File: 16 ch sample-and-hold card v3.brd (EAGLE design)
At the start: 77.2 x 24.8 mm, 32 parts, among them IC2 TL074D, IC3 TL074D, IC4 TL074D, IC5 TL074D, IC6 DG408DY, IC7 DG408DY

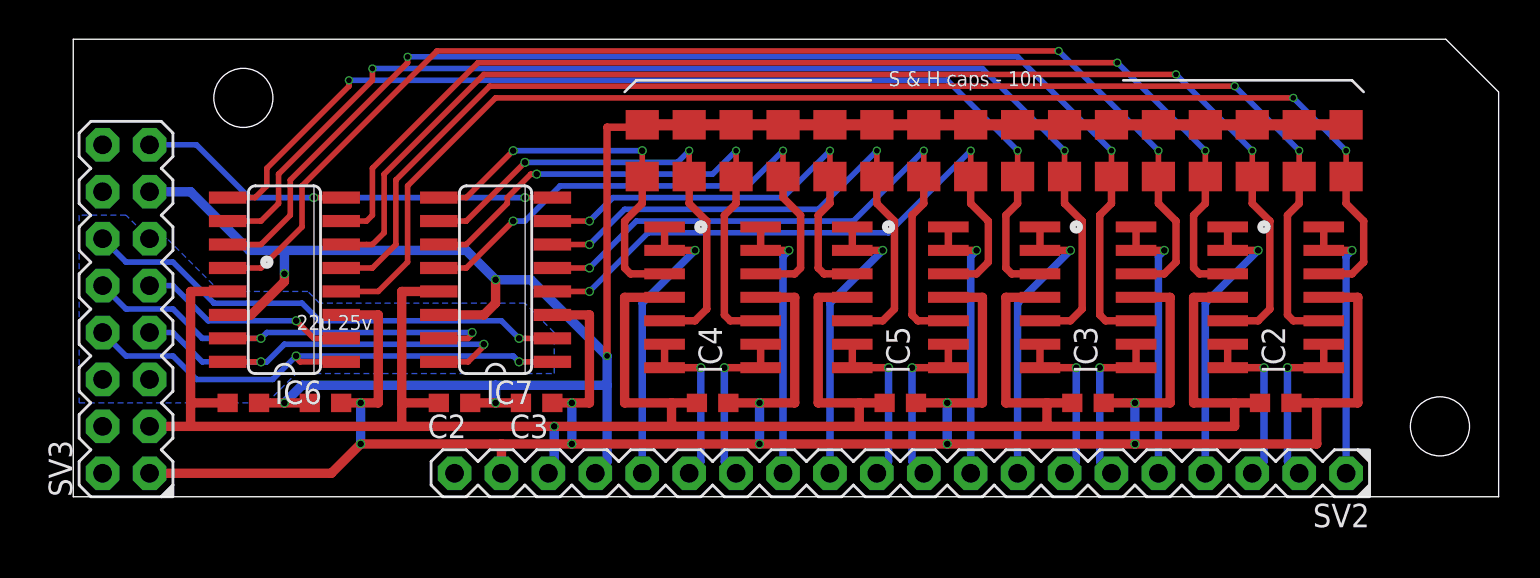
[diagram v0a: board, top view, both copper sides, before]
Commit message: Completed silk etc
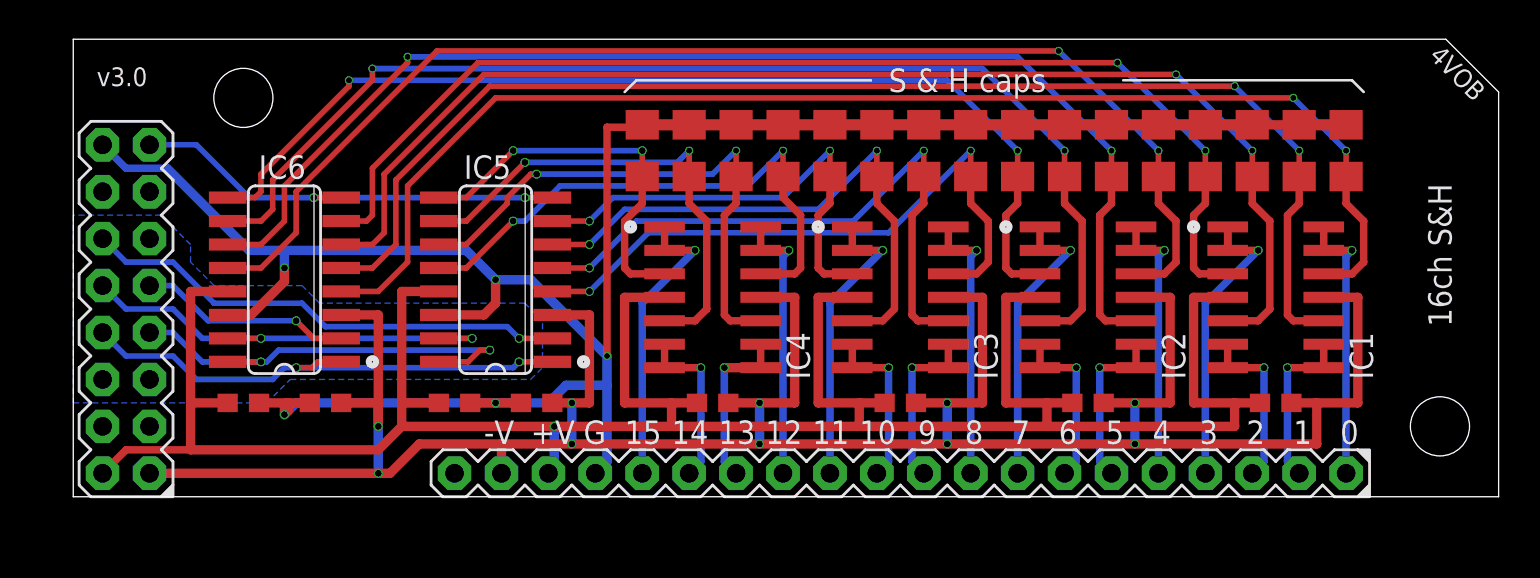
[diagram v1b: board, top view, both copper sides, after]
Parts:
- removed IC7: DG408DY, maxim:SO16
- added IC1: TL074D, linear:SO14
- added U$1: (no value), joakim:XONIK_LOGO_50
- IC5: value TL074D -> DG408DY; device linear:SO14 -> maxim:SO16
- moved IC5 21.9 mm to (22.5, 11.7), turned to 90 degrees
- moved IC2 10.2 mm to (54.6, 10.8)
- moved IC3 10.2 mm to (44.5, 10.8)
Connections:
- net OUT24 renamed OUT_12
- net OUT25 renamed OUT_13
- net OUT30 renamed OUT_14
- net OUT31 renamed OUT_15
- removed net IN1: C4.2, IC2.12, IC6.4
- removed net IN11: C9.2, IC3.10, IC6.11
- removed net IN12: C10.2, IC3.5, IC6.10
- removed net IN14: C11.2, IC3.3, IC6.9
- removed net IN17: C26.2, IC5.12, IC7.4
- removed net IN19: C27.2, IC5.10, IC7.5
- removed net IN20: C28.2, IC5.5, IC7.6
- removed net IN22: C29.2, IC5.3, IC7.7
- removed net IN25: C22.2, IC4.12, IC7.12
- removed net IN27: C23.2, IC4.10, IC7.11
- removed net IN28: C24.2, IC4.5, IC7.10
- removed net IN3: C5.2, IC2.10, IC6.5
- removed net IN30: C25.2, IC4.3, IC7.9
- removed net IN4: C6.2, IC2.5, IC6.6
- removed net IN6: C7.2, IC2.3, IC6.7
- removed net IN9: C8.2, IC3.12, IC6.12
- removed net N$1: SV3.16
- removed net N$15: SV3.4
- removed net N$16: SV3.2
- removed net N$3: SV3.14
- removed net OUT0: IC2.13, IC2.14, SV2.1
- removed net OUT1: IC2.8, IC2.9, SV2.2
- removed net OUT14: IC3.6, IC3.7, SV2.7
- removed net OUT15: IC3.1, IC3.2, SV2.8
- removed net OUT16: IC5.13, IC5.14, SV2.9
- removed net OUT17: IC5.8, IC5.9, SV2.10
- removed net OUT22: IC5.6, IC5.7, SV2.11
- removed net OUT23: IC5.1, IC5.2, SV2.12
- removed net OUT6: IC2.6, IC2.7, SV2.3
- removed net OUT7: IC2.1, IC2.2, SV2.4
- removed net OUT8: IC3.13, IC3.14, SV2.5
- removed net OUT9: IC3.8, IC3.9, SV2.6
- new net IN_0: C4.2, IC1.12, IC6.4
- new net IN_1: C5.2, IC1.10, IC6.5
- new net IN_10: C28.2, IC3.5, IC5.6
- new net IN_11: C29.2, IC3.3, IC5.7
- new net IN_12: C22.2, IC4.12, IC5.12
- new net IN_13: C23.2, IC4.10, IC5.11
- new net IN_14: C24.2, IC4.5, IC5.10
- new net IN_15: C25.2, IC4.3, IC5.9
- new net IN_2: C6.2, IC1.5, IC6.6
- new net IN_3: C7.2, IC1.3, IC6.7
- new net IN_4: C8.2, IC2.12, IC6.12
- new net IN_5: C9.2, IC2.10, IC6.11
- new net IN_6: C10.2, IC2.5, IC6.10
- new net IN_7: C11.2, IC2.3, IC6.9
- new net IN_8: C26.2, IC3.12, IC5.4
- new net IN_9: C27.2, IC3.10, IC5.5
- new net OUT_0: IC1.13, IC1.14, SV2.1
- new net OUT_1: IC1.8, IC1.9, SV2.2
- new net OUT_10: IC3.6, IC3.7, SV2.11
- new net OUT_11: IC3.1, IC3.2, SV2.12
- new net OUT_2: IC1.6, IC1.7, SV2.3
- new net OUT_3: IC1.1, IC1.2, SV2.4
- new net OUT_4: IC2.13, IC2.14, SV2.5
- new net OUT_5: IC2.8, IC2.9, SV2.6
- new net OUT_6: IC2.6, IC2.7, SV2.7
- new net OUT_7: IC2.1, IC2.2, SV2.8
- new net OUT_8: IC3.13, IC3.14, SV2.9
- new net OUT_9: IC3.8, IC3.9, SV2.10
- net +15V: now also IC1.4, IC5.13, SV3.2; no longer IC5.4, IC7.13, SV3.3
- net -15V: now also IC1.11, IC5.3; no longer IC5.11, IC7.3
- net A0: now also IC5.1; no longer IC7.1
- net A1: now also IC5.16; no longer IC7.16
- net A2: now also IC5.15; no longer IC7.15
- net AGND: now also IC5.14, SV3.16; no longer IC7.14, SV3.13
- net DAC: now also IC5.8; no longer IC7.8
- net EN2: now also IC5.2; no longer IC7.2
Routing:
- net IN_0: track 0.00 -> 71.2 mm, vias 0 -> 2
- net IN1: track 71.2 -> 0.00 mm, vias 2 -> 0
- net IN_1: track 0.00 -> 70.7 mm, vias 0 -> 2
- net IN3: track 70.7 -> 0.00 mm, vias 2 -> 0
- net IN_2: track 0.00 -> 68.2 mm, vias 0 -> 2
- net IN4: track 68.2 -> 0.00 mm, vias 2 -> 0
- net IN_4: track 0.00 -> 67.6 mm, vias 0 -> 2
- net IN9: track 67.6 -> 0.00 mm, vias 2 -> 0
- net IN_5: track 0.00 -> 66.7 mm, vias 0 -> 2
- net IN11: track 66.7 -> 0.00 mm, vias 2 -> 0
- net IN_6: track 0.00 -> 63.4 mm, vias 0 -> 2
- net IN12: track 63.4 -> 0.00 mm, vias 2 -> 0
- net IN_3: track 0.00 -> 62.4 mm, vias 0 -> 2
- net IN6: track 62.4 -> 0.00 mm, vias 2 -> 0
- net IN_7: track 0.00 -> 56.3 mm, vias 0 -> 2
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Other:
- board text added: "+"
- board text added: "+V"
- board text added: "-"
- board text added: "-V"
- board text added: "0"
- board text added: "1"
- board text added: "10"
- board text added: "11"
- board text added: "12"
- board text added: "13"
- board text added: "14"
- board text added: "15"
- board text added: "16ch S&H"
- board text added: "2"
- board text added: "3"
- board text added: "4"
- board text added: "4VOB"
- board text added: "5"
- board text added: "6"
- board text added: "7"
- board text added: "8"
- board text added: "9"
- board text added: "A0"
- board text added: "A1"
- board text added: "A2"
- board text added: "D"
- board text added: "DGND"
- board text added: "E0"
- board text added: "E1"
- board text added: "G"
- board text added: "S & H caps"
- board text added: "v3.0"
- board text removed: "0.1u"
- board text removed: "22u 25v"
- board text removed: "S & H caps - 10n"
